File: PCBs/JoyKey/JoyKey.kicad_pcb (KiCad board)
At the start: 2 copper layers, 100 x 56.8 mm, 50 parts, among them J1 OLED_DISPLAY, J2 Conn_01x03_Socket, J3 Testpad wire hole1, J4 JST PH, J5 Top Trigger 1, J6 Top Trigger 2, Q1 PMOS,Si7157DP, SW1 RotaryEncoder_Switch, SW2 SW_Push_45deg, SW3 SW_Push_45deg, SW4 SW_Push_45deg, SW5 SW_Push_45deg, SW6 SW_Push_45deg, SW7 SW_Push_45deg, U1 BQ25060, U3 XIAO-RP2040-DIP, U4 LP2981-3.3, U5 2_axis_analog_joystick_button

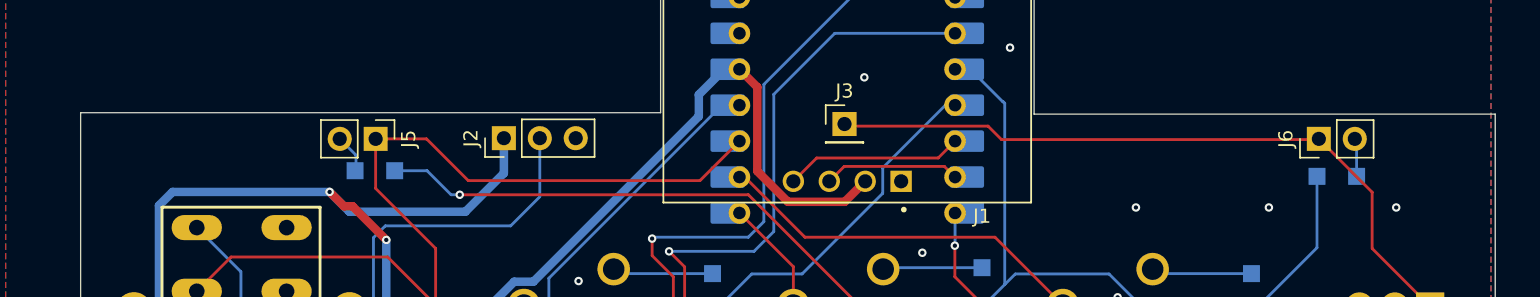
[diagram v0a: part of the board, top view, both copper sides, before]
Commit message: Add 2 mounting holes
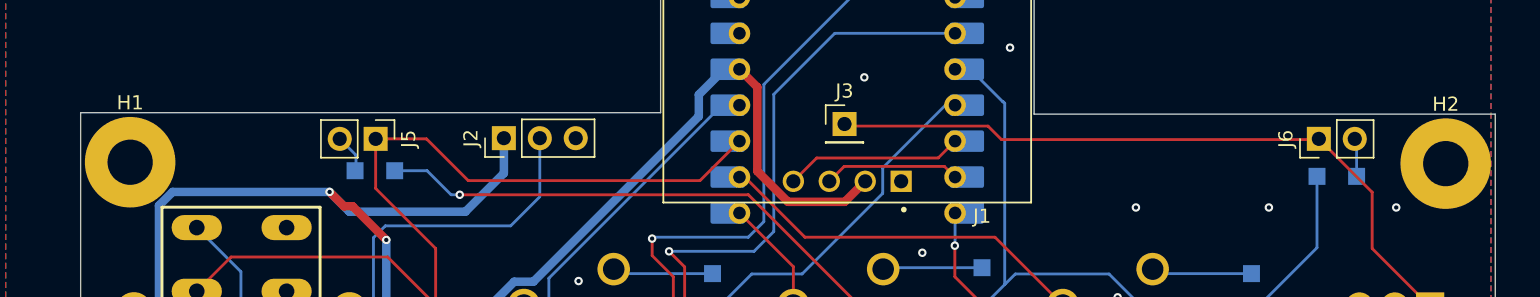
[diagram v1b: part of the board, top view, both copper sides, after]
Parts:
- added H1: MountingHole, MountingHole:MountingHole_3.2mm_M3_Pad, F.Cu at (89.8, 96.9)
- added H2: MountingHole, MountingHole:MountingHole_3.2mm_M3_Pad, F.Cu at (182.8, 97.0)
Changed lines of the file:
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@@
+		)
+	)
+	(footprint "MountingHole:MountingHole_3.2mm_M3_Pad"
+		(layer "F.Cu")
+		(at 182.8 97)
+		(descr "Mounting Hole 3.2mm, M3")
+		(tags "mounting hole 3.2mm m3")
+		(property "Reference" "H2"
+			(at 0 -4.2 0)
+			(layer "F.SilkS")
+			(effects
+				(font
+					(size 1 1)
+					(thickness 0.15)
+				)
+			)
+		)
+		(property "Value" "MountingHole"
+			(at 0 4.2 0)
+			(layer "F.Fab")
+			(effects
+				(font
+					(size 1 1)
+					(thickness 0.15)
+				)
+			)
+		)
+		(property "Footprint" "MountingHole:MountingHole_3.2mm_M3_Pad"
+			(at 0 0 0)
+			(unlocked yes)
+			(layer "F.Fab")
+			(hide yes)
+			(effects
+				(font
+					(size 1.27 1.27)
+					(thickness 0.15)
+				)
+			)
+		)
+		(property "Datasheet" ""
+			(at 0 0 0)
+			(unlocked yes)
+			(layer "F.Fab")
+			(hide yes)
+			(effects
+				(font
+					(size 1.27 1.27)
+					(thickness 0.15)
+				)
+			)
+		)
+		(property "Description" "Mounting Hole without connection"
+			(at 0 0 0)
+			(unlocked yes)
+			(layer "F.Fab")
+			(hide yes)
+			(effects
+				(font
+					(size 1.27 1.27)
+					(thickness 0.15)
+				)
+			)
+		)
+		(property ki_fp_filters "MountingHole*")
+		(sheetname "Root")
+		(sheetfile "JoyKey.kicad_sch")
+		(attr exclude_from_pos_files exclude_from_bom)
+		(fp_circle
+			(center 0 0)
+			(end 3.2 0)
+			(stroke
+				(width 0.15)
+				(type solid)
+			)
+			(fill none)
+			(layer "Cmts.User")
+		)
+		(fp_circle
+			(center 0 0)
+			(end 3.45 0)
+			(stroke
+				(width 0.05)
+				(type solid)
+			)
+			(fill none)
+			(layer "F.CrtYd")
+		)
+		(fp_text user "${REFERENCE}"
+			(at 0 0 0)
+			(layer "F.Fab")
+			(effects
+				(font
+					(size 1 1)
+					(thickness 0.15)
+				)
+			)
+		)
+		(pad "1" thru_hole circle
+			(at 0 0)
+			(size 6.4 6.4)
+			(drill 3.2)
+			(layers "*.Cu" "*.Mask")
+			(remove_unused_layers no)
+		)
+	)
+	(footprint "MountingHole:MountingHole_3.2mm_M3_Pad"
+		(layer "F.Cu")
+		(at 89.8 96.9)
+		(descr "Mounting Hole 3.2mm, M3")
+		(tags "mounting hole 3.2mm m3")
+		(property "Reference" "H1"
+			(at 0 -4.2 0)
+			(layer "F.SilkS")
+			(effects
+				(font
+					(size 1 1)
+					(thickness 0.15)
+				)
+			)
+		)
+		(property "Value" "MountingHole"
+			(at 0 4.2 0)
+			(layer "F.Fab")
+			(effects
+				(font
+					(size 1 1)
+					(thickness 0.15)
+				)
+			)
+		)
+		(property "Footprint" "MountingHole:MountingHole_3.2mm_M3_Pad"
+			(at 0 0 0)
+			(unlocked yes)
+			(layer "F.Fab")
+			(hide yes)
+			(effects
+				(font
+					(size 1.27 1.27)
+					(thickness 0.15)
+				)
+			)
+		)
+		(property "Datasheet" ""
+			(at 0 0 0)
+			(unlocked yes)
+			(layer "F.Fab")
+			(hide yes)
+			(effects
+				(font
+					(size 1.27 1.27)
+					(thickness 0.15)
+				)
+			)
+		)
+		(property "Description" "Mounting Hole without connection"
+			(at 0 0 0)
+			(unlocked yes)
+			(layer "F.Fab")
+			(hide yes)
+			(effects
+				(font
+					(size 1.27 1.27)
+					(thickness 0.15)
+				)
+			)
+		)
+		(property ki_fp_filters "MountingHole*")
+		(sheetname "Root")
+		(sheetfile "JoyKey.kicad_sch")
+		(attr exclude_from_pos_files exclude_from_bom)
+		(fp_circle
+			(center 0 0)
+			(end 3.2 0)
+			(stroke
+				(width 0.15)
+				(type solid)
+			)
+			(fill none)
+			(layer "Cmts.User")
+		)
+		(fp_circle
+			(center 0 0)
+			(end 3.45 0)
+			(stroke
+				(width 0.05)
+				(type solid)
+			)
+			(fill none)
+			(layer "F.CrtYd")
+		)
+		(fp_text user "${REFERENCE}"
+			(at 0 0 0)
+			(layer "F.Fab")
+			(effects
+				(font
+					(size 1 1)
+					(thickness 0.15)
+				)
+			)
+		)
+		(pad "1" thru_hole circle
+			(at 0 0)
+			(size 6.4 6.4)
+			(drill 3.2)
+			(layers "*.Cu" "*.Mask")
+			(remove_unused_layers no)
 		)
 	)

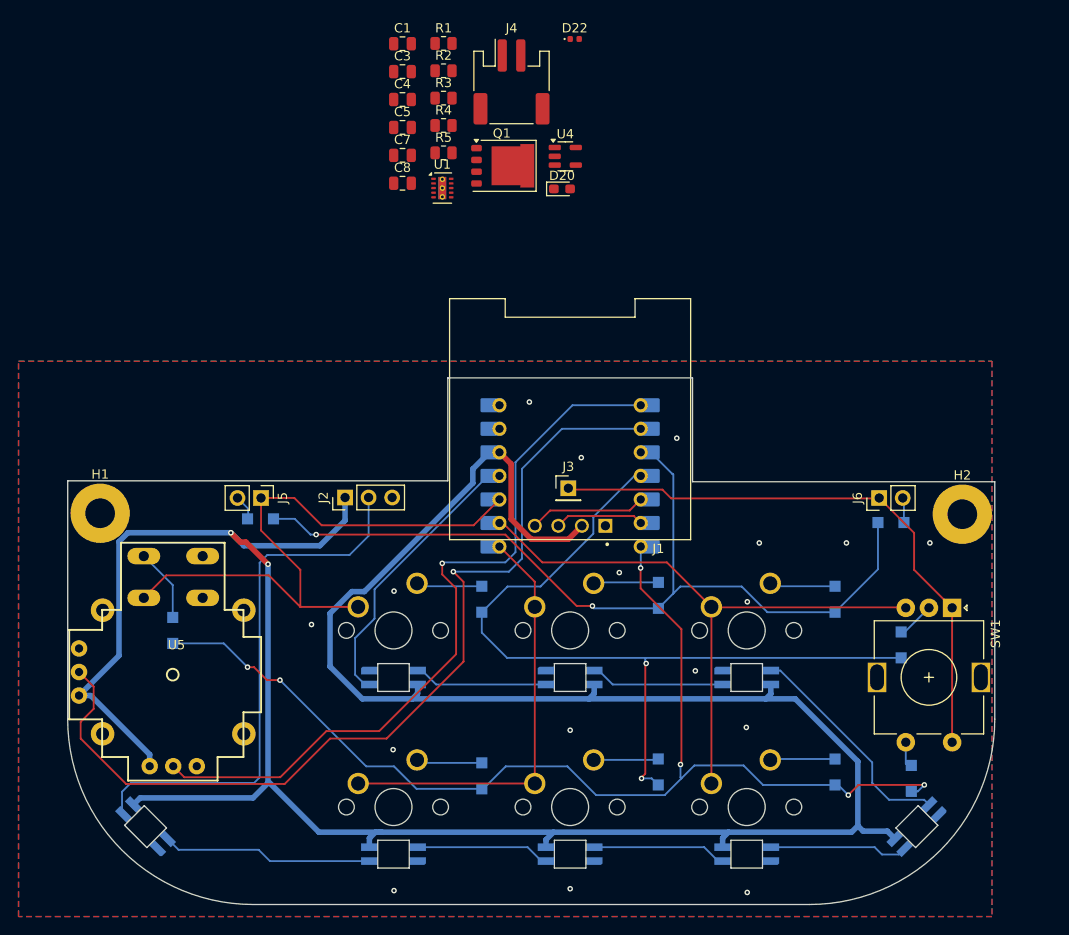
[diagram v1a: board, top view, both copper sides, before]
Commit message: Added filleted lines and CAD export
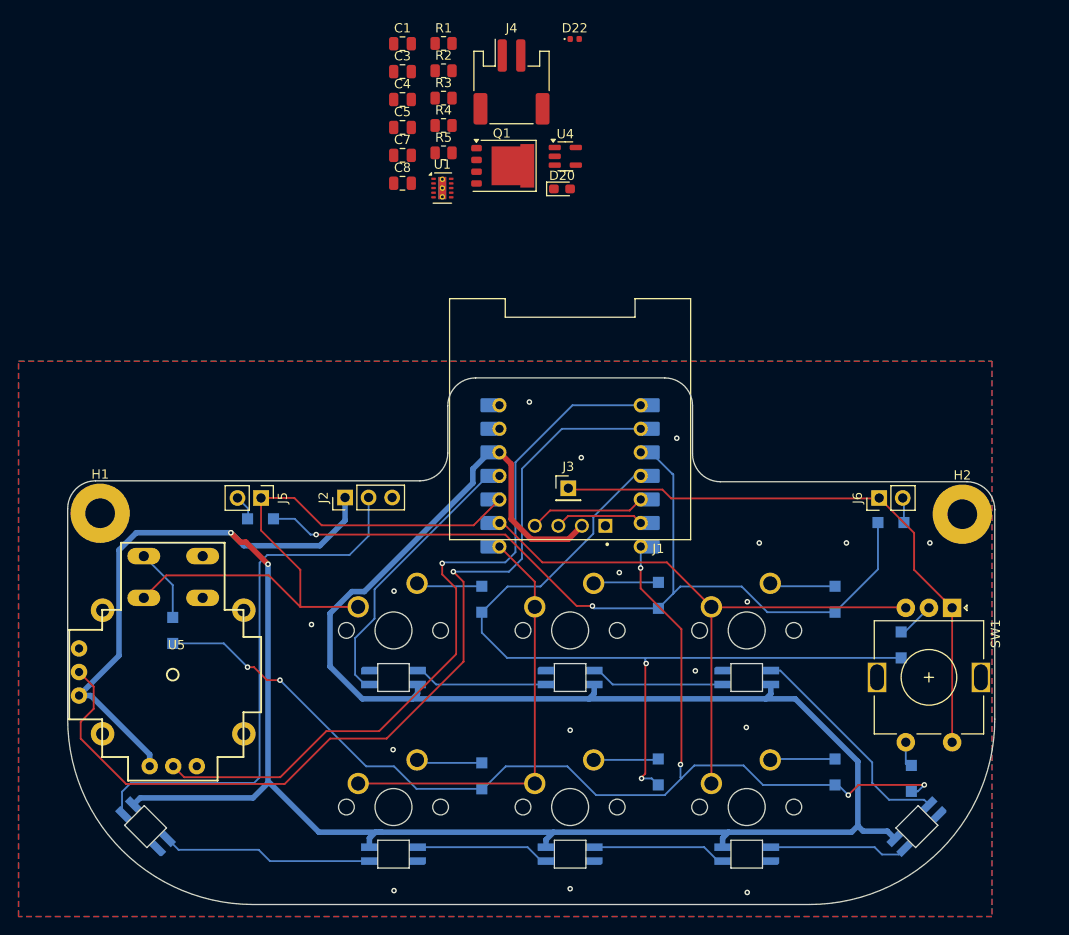
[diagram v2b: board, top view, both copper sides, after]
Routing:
- net +3V3: track 302.6 -> 302.0 mm
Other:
- outline, holes or cut-outs redrawn

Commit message: Added Silkscreen name and author
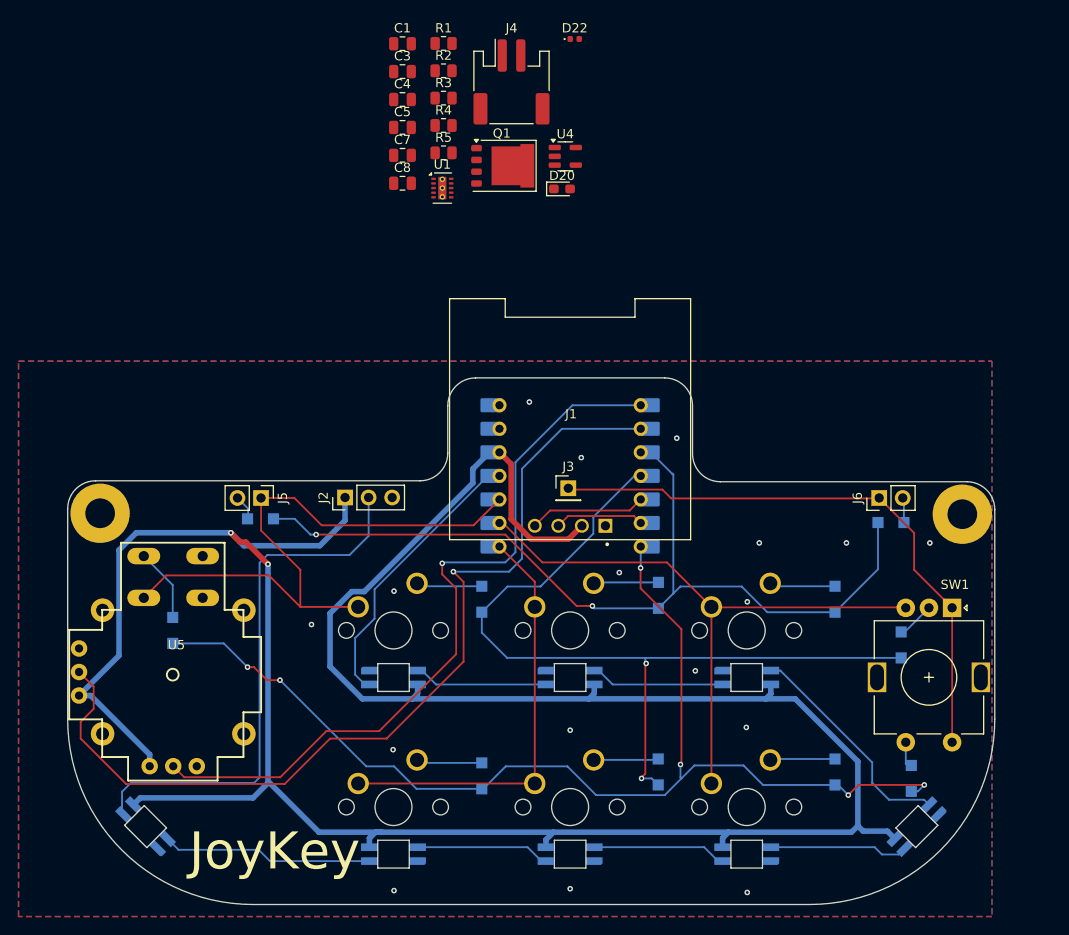
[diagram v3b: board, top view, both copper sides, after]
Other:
- board text added: "Designed by Asher Edwards"
- board text added: "JoyKey"
- board text added: "Xiao This Side"
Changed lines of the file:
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@@
 		(at 140.49375 86.75 180)
 		(property "Reference" "J1"
-			(at -9.525 -13.97 0)
+			(at -0.10625 0.55 0)
 			(layer "F.SilkS")
 			(effects
@@
 			(at 0 -4.2 0)
 			(layer "F.SilkS")
+			(hide yes)
 			(effects
 				(font
@@
 			(at 0 -4.2 0)
 			(layer "F.SilkS")
+			(hide yes)
 			(effects
 				(font
@@
 		(tags "rotary encoder")
 		(property "Reference" "SW1"
-			(at 2.8 -4.7 90)
+			(at -2.5 -0.3 180)
 			(layer "F.SilkS")
 			(effects
@@
 		(at 140.49375 92.86875 180)
 		(property "Reference" "U3"
-			(at -8.5 12 0)
+			(at -2.90625 1.66875 0)
 			(unlocked yes)
 			(layer "B.SilkS")
@@
 		(layer "Edge.Cuts")
 	)
+	(gr_text "Designed by Asher Edwards"
+		(at 156.6 138.2 0)
+		(layer "B.SilkS" knockout)
+		(effects
+			(font
+				(size 1.5 1.5)
+				(thickness 0.3)
+			)
+			(justify left bottom mirror)
+		)
+	)
 	(gr_text "12mm"
 		(at 114.173 126.111 -90)
@@
 		)
 	)
+	(gr_text "Xiao This Side"
+		(at 145.9 88.6 0)
+		(layer "B.SilkS")
+		(effects
+			(font
+				(size 1 1)
+				(thickness 0.1)
+			)
+			(justify left bottom mirror)
+		)
+	)
+	(gr_text "JoyKey"
+		(at 99.4 135.7 0)
+		(layer "F.SilkS")
+		(effects
+			(font
+				(face "Mitra")
+				(size 4 4)
+				(thickness 0.1)
+			)
+			(justify left bottom)
+		)
+		(render_cache "JoyKey" 0
+			(polygon
+				(pts
+					(xy 99.587578 134.022512) (xy 100.025261 133.96487) (xy 100.035462 134.165214) (xy 100.075636 134.357185)
+					(xy 100.154221 134.500251) (xy 100.320128 134.613072) (xy 100.51277 134.644842) (xy 100.707783 134.614312)
+					(xy 100.806838 134.566685) (xy 100.94493 134.425565) (xy 100.977808 134.354682) (xy 101.016517 134.153101)
+					(xy 101.025633 133.944074) (xy 101.02568 133.925792) (xy 101.02568 131.58106) (xy 101.463363 131.58106)
+					(xy 101.463363 133.883782) (xy 101.45683 134.083572) (xy 101.43386 134.28031) (xy 101.383328 134.480467)
+					(xy 101.358827 134.54226) (xy 101.255014 134.714227) (xy 101.111859 134.84911) (xy 101.032519 134.898855)
+					(xy 100.839429 134.977291) (xy 100.638295 135.014203) (xy 100.510816 135.02) (xy 100.29979 135.004307)
+					(xy 100.093916 134.949138) (xy 99.921427 134.854246) (xy 99.824982 134.768918) (xy 99.710221 134.607969)
+					(xy 99.633019 134.40869) (xy 99.595924 134.199374)
+				)
+			)
+			(polygon
+				(pts
+					(xy 103.952417 132.472275) (xy 104.147737 132.519819) (xy 104.349665 132.612967) (xy 104.507719 132.728432)
+					(xy 104.570132 132.78762) (xy 104.696516 132.944198) (xy 104.791859 133.124992) (xy 104.85616 133.330002)
+					(xy 104.886568 133.525) (xy 104.894487 133.701088) (xy 104.887568 133.898806) (xy 104.862716 134.101298)
+					(xy 104.813154 134.299178) (xy 104.749895 134.448471) (xy 104.63525 134.621877) (xy 104.490127 134.76596)
+					(xy 104.331751 134.8715) (xy 104.138374 134.956046) (xy 103.934376 135.005498) (xy 103.739706 135.02)
+					(xy 103.520805 135.004245) (xy 103.321444 134.956981) (xy 103.141625 134.878208) (xy 102.960046 134.749599)
+					(xy 102.898534 134.69076) (xy 102.774815 134.532219) (xy 102.681482 134.345534) (xy 102.618537 134.130707)
+					(xy 102.58877 133.924169) (xy 102.581058 133.737236) (xy 102.955198 133.737236) (xy 102.964922 133.932703)
+					(xy 102.999849 134.128158) (xy 103.069504 134.312428) (xy 103.158408 134.444563) (xy 103.31093 134.577501)
+					(xy 103.506545 134.65959) (xy 103.673272 134.67806) (xy 103.874836 134.650353) (xy 104.065757 134.55693)
+					(xy 104.189113 134.443586) (xy 104.297305 134.272006) (xy 104.360417 134.075818) (xy 104.389268 133.868211)
+					(xy 104.394277 133.722581) (xy 104.381393 133.509174) (xy 104.336099 133.301935) (xy 104.247523 133.112456)
+					(xy 104.188136 133.033817) (xy 104.034293 132.899766) (xy 103.838815 132.816991) (xy 103.673272 132.798367)
+					(xy 103.471824 132.825842) (xy 103.281292 132.918486) (xy 103.158408 133.030886) (xy 103.051247 133.199776)
+					(xy 102.988736 133.392074) (xy 102.96016 133.595055) (xy 102.955198 133.737236) (xy 102.581058 133.737236)
+					(xy 102.581018 133.736259) (xy 102.590297 133.532073) (xy 102.625926 133.309782) (xy 102.688276 133.112288)
+					(xy 102.794792 132.913222) (xy 102.937679 132.747908) (xy 102.96106 132.727048) (xy 103.12916 132.608651)
+					(xy 103.314968 132.524082) (xy 103.518483 132.47334) (xy 103.739706 132.456427)
+				)
+			)
+			(polygon
+				(pts
+					(xy 105.697557 135.976454) (xy 105.650662 135.607159) (xy 105.842908 135.643438) (xy 105.889043 135.645261)
+					(xy 106.083506 135.611876) (xy 106.110816 135.598367) (xy 106.246615 135.469406) (xy 106.329825 135.281327)
+					(xy 106.375575 135.155799) (xy 106.410746 135.053217) (xy 105.478715 132.581479) (xy 105.927145 132.581479)
+					(xy 106.438101 134.009811) (xy 106.504953 134.200439) (xy 106.565802 134.397531) (xy 106.61591 134.582316)
+					(xy 106.668405 134.385465) (xy 106.727827 134.192539) (xy 106.787857 134.020558) (xy 107.313468 132.581479)
+					(xy 107.72575 132.581479) (xy 106.79665 135.069825) (xy 106.725514 135.256304) (xy 106.648101 135.445097)
+					(xy 106.5612 135.626699) (xy 106.449215 135.794081) (xy 106.30621 135.925652) (xy 106.117667 136.004778)
+					(xy 105.965247 136.020418) (xy 105.770708 135.995689)
+				)
+			)
+			(polygon
+				(pts
+					(xy 108.06769 135.02) (xy 108.06769 131.643586) (xy 108.505373 131.643586) (xy 108.505373 133.317138)
+					(xy 110.186741 131.643586) (xy 110.794417 131.643586) (xy 109.371946 133.011346) (xy 110.856943 135.02)
+					(xy 110.263921 135.02) (xy 109.057362 133.311277) (xy 108.505373 133.848611) (xy 108.505373 135.02)
+				)
+			)
+			(polygon
+				(pts
+					(xy 112.471489 132.472321) (xy 112.684683 132.529413) (xy 112.87565 132.628026) (xy 113.044391 132.768161)
+					(xy 113.063921 132.788597) (xy 113.184976 132.946871) (xy 113.276298 133.131044) (xy 113.337887 133.341117)
+					(xy 113.367013 133.541793) (xy 113.374598 133.723558) (xy 113.374598 133.832002) (xy 111.561339 133.832002)
+					(xy 111.577491 134.04672) (xy 111.633323 134.250129) (xy 111.740801 134.431122) (xy 111.765526 134.459218)
+					(xy 111.919044 134.583812) (xy 112.114958 134.660749) (xy 112.281367 134.67806) (xy 112.480606 134.651226)
+					(xy 112.661896 134.563451) (xy 112.672156 134.555938) (xy 112.811217 134.410323) (xy 112.907774 134.233767)
+					(xy 112.933007 134.170034) (xy 113.360921 134.221814) (xy 113.291034 134.422536) (xy 113.193481 134.596055)
+					(xy 113.05264 134.75695) (xy 112.986741 134.811905) (xy 112.800982 134.921642) (xy 112.608512 134.985656)
+					(xy 112.392086 135.016748) (xy 112.288206 135.02) (xy 112.064543 135.004151) (xy 111.86201 134.956607)
+					(xy 111.680608 134.877366) (xy 111.499166 134.747994) (xy 111.438241 134.688806) (xy 111.315663 134.5311)
+					(xy 111.223193 134.347774) (xy 111.160829 134.13883) (xy 111.131336 133.939345) (xy 111.123656 133.758729)
+					(xy 111.134819 133.536541) (xy 111.142496 133.490062) (xy 111.582833 133.490062) (xy 112.937892 133.490062)
+					(xy 112.903087 133.283295) (xy 112.826365 133.097285) (xy 112.781577 133.035771) (xy 112.629475 132.900608)
+					(xy 112.449899 132.821551) (xy 112.262805 132.798367) (xy 112.059106 132.824882) (xy 111.8682 132.913452)
+					(xy 111.778227 132.986922) (xy 111.659159 133.145604) (xy 111.595045 133.34028) (xy 111.582833 133.490062)
+					(xy 111.142496 133.490062) (xy 111.168307 133.333793) (xy 111.235593 133.121823) (xy 111.333266 132.936314)
+					(xy 111.441172 132.798367) (xy 111.589201 132.66513) (xy 111.780703 132.552931) (xy 111.967801 132.489819)
+					(xy 112.173132 132.459432) (xy 112.266713 132.456427)
+				)
+			)
+			(polygon
+				(pts
+					(xy 114.302721 135.976454) (xy 114.255826 135.607159) (xy 114.448072 135.643438) (xy 114.494207 135.645261)
+					(xy 114.68867 135.611876) (xy 114.71598 135.598367) (xy 114.851779 135.469406) (xy 114.934989 135.281327)
+					(xy 114.980739 135.155799) (xy 115.01591 135.053217) (xy 114.083879 132.581479) (xy 114.532309 132.581479)
+					(xy 115.043265 134.009811) (xy 115.110117 134.200439) (xy 115.170966 134.397531) (xy 115.221074 134.582316)
+					(xy 115.273569 134.385465) (xy 115.332991 134.192539) (xy 115.393021 134.020558) (xy 115.918632 132.581479)
+					(xy 116.330914 132.581479) (xy 115.401814 135.069825) (xy 115.330678 135.256304) (xy 115.253265 135.445097)
+					(xy 115.166364 135.626699) (xy 115.054379 135.794081) (xy 114.911374 135.925652) (xy 114.722831 136.004778)
+					(xy 114.570411 136.020418) (xy 114.375872 135.995689)
+				)
+			)
+		)
+	)
